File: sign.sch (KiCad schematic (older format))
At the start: 142 parts, among them J1 CONN_01X02, J2 CONN_01X02, J3 CONN_01X02, U1 APA102C_x6, U10 APA102C_x2, U100 APA102C_x6, U101 APA102C_x4, U102 APA102C_x2, U103 APA102C_x1, U104 APA102C_x3, U105 APA102C_x5, U106 APA102C_x2, U107 APA102C_x3, U108 APA102C_x10, U109 APA102C_x9, U11 APA102C_x2, U110 APA102C_x3, U111 APA102C_x12, U112 APA102C_x16, U113 APA102C_x8, U114 APA102C_x13, U115 APA102C_x3, U116 APA102C_x6, U117 APA102C_x3, U118 APA102C_x6, U119 APA102C_x3, U12 APA102C_x2, U120 APA102C_x2, U121 APA102C_x6, U122 APA102C_x3, U123 APA102C_x6, U124 APA102C_x7, U125 APA102C_x12, U126 APA102C_x6, U127 APA102C_x11, U128 APA102C_x4, U129 APA102C_x6, U13 APA102C_x2, U130 APA102C_x2, U131 APA102C_x2, U132 APA102C_x3, U133 APA102C_x1, U134 APA102C_x3, U135 APA102C_x3, U136 APA102C_x12, U137 APA102C_x12, U138 APA102C_x9, U139 APA102C_x4, U14 APA102C_x3, U15 APA102C_x3, U16 APA102C_x3, U17 APA102C_x3, U18 APA102C_x5, U19 APA102C_x6, U2 APA102C_x8, U20 APA102C_x2, U21 APA102C_x7, U22 APA102C_x5, U23 APA102C_x7, U24 APA102C_x3, U25 APA102C_x2, U26 APA102C_x7, U27 APA102C_x2, U28 APA102C_x3, U29 APA102C_x5, U3 APA102C_x11, U30 APA102C_x2, U31 APA102C_x5, U32 APA102C_x2, U33 APA102C_x8, U34 APA102C_x9, U35 APA102C_x3, U36 APA102C_x2, U37 APA102C_x5, U38 APA102C_x11, U39 APA102C_x6, U4 APA102C_x6, U40 APA102C_x4, U41 APA102C_x5, U42 APA102C_x3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

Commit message: Start auto-generating PCB layout.
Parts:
- removed J1, J2, J3: CONN_01X02, symbol CONN_01X02
- removed U1: APA102C_x6, symbol APA102C_x6
- added U139: APA102C_x4, symbol APA102C_x4
- U1: renamed from U2; value APA102C_x8 -> APA102C_x6; symbol APA102C_x8 -> APA102C_x6
- U100: renamed from U101; value APA102C_x4 -> APA102C_x6; symbol APA102C_x4 -> APA102C_x6
- U101: renamed from U102; value APA102C_x2 -> APA102C_x4; symbol APA102C_x2 -> APA102C_x4
- U102: renamed from U103; value APA102C_x1 -> APA102C_x2; symbol APA102C_x1 -> APA102C_x2
- U103: renamed from U104; value APA102C_x3 -> APA102C_x1; symbol APA102C_x3 -> APA102C_x1
- U104: renamed from U105; value APA102C_x5 -> APA102C_x3; symbol APA102C_x5 -> APA102C_x3
- U105: renamed from U106; value APA102C_x2 -> APA102C_x5; symbol APA102C_x2 -> APA102C_x5
- U106: renamed from U107; value APA102C_x3 -> APA102C_x2; symbol APA102C_x3 -> APA102C_x2
- U107: renamed from U108; value APA102C_x10 -> APA102C_x3; symbol APA102C_x10 -> APA102C_x3
- U108: renamed from U109; value APA102C_x9 -> APA102C_x10; symbol APA102C_x9 -> APA102C_x10
- U109: renamed from U110; value APA102C_x3 -> APA102C_x9; symbol APA102C_x3 -> APA102C_x9
- U110: renamed from U111; value APA102C_x12 -> APA102C_x3; symbol APA102C_x12 -> APA102C_x3
- U111: renamed from U112; value APA102C_x16 -> APA102C_x12; symbol APA102C_x16 -> APA102C_x12
- U112: renamed from U113; value APA102C_x8 -> APA102C_x16; symbol APA102C_x8 -> APA102C_x16
- U113: renamed from U114; value APA102C_x13 -> APA102C_x8; symbol APA102C_x13 -> APA102C_x8
- U114: renamed from U115; value APA102C_x3 -> APA102C_x13; symbol APA102C_x3 -> APA102C_x13
- U115: renamed from U116; value APA102C_x6 -> APA102C_x3; symbol APA102C_x6 -> APA102C_x3
- U116: renamed from U117; value APA102C_x3 -> APA102C_x6; symbol APA102C_x3 -> APA102C_x6
- U117: renamed from U118; value APA102C_x6 -> APA102C_x3; symbol APA102C_x6 -> APA102C_x3
- U118: renamed from U119; value APA102C_x3 -> APA102C_x6; symbol APA102C_x3 -> APA102C_x6
- U119: renamed from U120; value APA102C_x2 -> APA102C_x3; symbol APA102C_x2 -> APA102C_x3
- U120: renamed from U121; value APA102C_x6 -> APA102C_x2; symbol APA102C_x6 -> APA102C_x2
- U121: renamed from U122; value APA102C_x3 -> APA102C_x6; symbol APA102C_x3 -> APA102C_x6
- U122: renamed from U123; value APA102C_x6 -> APA102C_x3; symbol APA102C_x6 -> APA102C_x3
- U123: renamed from U124; value APA102C_x7 -> APA102C_x6; symbol APA102C_x7 -> APA102C_x6
- U124: renamed from U125; value APA102C_x12 -> APA102C_x7; symbol APA102C_x12 -> APA102C_x7
- U125: renamed from U126; value APA102C_x6 -> APA102C_x12; symbol APA102C_x6 -> APA102C_x12
- U126: renamed from U127; value APA102C_x11 -> APA102C_x6; symbol APA102C_x11 -> APA102C_x6
- U127: renamed from U128; value APA102C_x4 -> APA102C_x11; symbol APA102C_x4 -> APA102C_x11
- U128: renamed from U129; value APA102C_x6 -> APA102C_x4; symbol APA102C_x6 -> APA102C_x4
- U129: renamed from U130; value APA102C_x2 -> APA102C_x6; symbol APA102C_x2 -> APA102C_x6
- U13: renamed from U14; value APA102C_x3 -> APA102C_x2; symbol APA102C_x3 -> APA102C_x2
- U131: renamed from U132; value APA102C_x3 -> APA102C_x2; symbol APA102C_x3 -> APA102C_x2
- U132: renamed from U133; value APA102C_x1 -> APA102C_x3; symbol APA102C_x1 -> APA102C_x3
- U133: renamed from U134; value APA102C_x3 -> APA102C_x1; symbol APA102C_x3 -> APA102C_x1
- U135: renamed from U136; value APA102C_x12 -> APA102C_x3; symbol APA102C_x12 -> APA102C_x3
- U137: renamed from U138; value APA102C_x9 -> APA102C_x12; symbol APA102C_x9 -> APA102C_x12
- U138: renamed from U139; value APA102C_x4 -> APA102C_x9; symbol APA102C_x4 -> APA102C_x9
- U17: renamed from U18; value APA102C_x5 -> APA102C_x3; symbol APA102C_x5 -> APA102C_x3
- U18: renamed from U19; value APA102C_x6 -> APA102C_x5; symbol APA102C_x6 -> APA102C_x5
- U19: renamed from U20; value APA102C_x2 -> APA102C_x6; symbol APA102C_x2 -> APA102C_x6
- U2: renamed from U3; value APA102C_x11 -> APA102C_x8; symbol APA102C_x11 -> APA102C_x8
- U20: renamed from U21; value APA102C_x7 -> APA102C_x2; symbol APA102C_x7 -> APA102C_x2
- U21: renamed from U22; value APA102C_x5 -> APA102C_x7; symbol APA102C_x5 -> APA102C_x7
- U22: renamed from U23; value APA102C_x7 -> APA102C_x5; symbol APA102C_x7 -> APA102C_x5
- U23: renamed from U24; value APA102C_x3 -> APA102C_x7; symbol APA102C_x3 -> APA102C_x7
- U24: renamed from U25; value APA102C_x2 -> APA102C_x3; symbol APA102C_x2 -> APA102C_x3
- U25: renamed from U26; value APA102C_x7 -> APA102C_x2; symbol APA102C_x7 -> APA102C_x2
- U26: renamed from U27; value APA102C_x2 -> APA102C_x7; symbol APA102C_x2 -> APA102C_x7
- U27: renamed from U28; value APA102C_x3 -> APA102C_x2; symbol APA102C_x3 -> APA102C_x2
- U28: renamed from U29; value APA102C_x5 -> APA102C_x3; symbol APA102C_x5 -> APA102C_x3
- U29: renamed from U30; value APA102C_x2 -> APA102C_x5; symbol APA102C_x2 -> APA102C_x5
- U3: renamed from U4; value APA102C_x6 -> APA102C_x11; symbol APA102C_x6 -> APA102C_x11
- U30: renamed from U31; value APA102C_x5 -> APA102C_x2; symbol APA102C_x5 -> APA102C_x2
- U31: renamed from U32; value APA102C_x2 -> APA102C_x5; symbol APA102C_x2 -> APA102C_x5
- U32: renamed from U33; value APA102C_x8 -> APA102C_x2; symbol APA102C_x8 -> APA102C_x2
- U33: renamed from U34; value APA102C_x9 -> APA102C_x8; symbol APA102C_x9 -> APA102C_x8
- U34: renamed from U35; value APA102C_x3 -> APA102C_x9; symbol APA102C_x3 -> APA102C_x9
- U35: renamed from U36; value APA102C_x2 -> APA102C_x3; symbol APA102C_x2 -> APA102C_x3
- U36: renamed from U37; value APA102C_x5 -> APA102C_x2; symbol APA102C_x5 -> APA102C_x2
- U37: renamed from U38; value APA102C_x11 -> APA102C_x5; symbol APA102C_x11 -> APA102C_x5
- U38: renamed from U39; value APA102C_x6 -> APA102C_x11; symbol APA102C_x6 -> APA102C_x11
- U39: renamed from U40; value APA102C_x4 -> APA102C_x6; symbol APA102C_x4 -> APA102C_x6
- U4: renamed from U5; value APA102C_x3 -> APA102C_x6; symbol APA102C_x3 -> APA102C_x6
- U40: renamed from U41; value APA102C_x5 -> APA102C_x4; symbol APA102C_x5 -> APA102C_x4
- U41: renamed from U42; value APA102C_x3 -> APA102C_x5; symbol APA102C_x3 -> APA102C_x5
- U42: renamed from U43; value APA102C_x4 -> APA102C_x3; symbol APA102C_x4 -> APA102C_x3
- U43: renamed from U44; value APA102C_x6 -> APA102C_x4; symbol APA102C_x6 -> APA102C_x4
- U44: renamed from U45; value APA102C_x4 -> APA102C_x6; symbol APA102C_x4 -> APA102C_x6
- U45: renamed from U46; value APA102C_x3 -> APA102C_x4; symbol APA102C_x3 -> APA102C_x4
- U46: renamed from U47; value APA102C_x4 -> APA102C_x3; symbol APA102C_x4 -> APA102C_x3
- U47: renamed from U48; value APA102C_x2 -> APA102C_x4; symbol APA102C_x2 -> APA102C_x4
- U48: renamed from U49; value APA102C_x3 -> APA102C_x2; symbol APA102C_x3 -> APA102C_x2
- U49: renamed from U50; value APA102C_x2 -> APA102C_x3; symbol APA102C_x2 -> APA102C_x3
- U51: renamed from U52; value APA102C_x3 -> APA102C_x2; symbol APA102C_x3 -> APA102C_x2
- U55: renamed from U56; value APA102C_x7 -> APA102C_x3; symbol APA102C_x7 -> APA102C_x3
- U56: renamed from U57; value APA102C_x4 -> APA102C_x7; symbol APA102C_x4 -> APA102C_x7
- U57: renamed from U58; value APA102C_x12 -> APA102C_x4; symbol APA102C_x12 -> APA102C_x4
- U58: renamed from U59; value APA102C_x3 -> APA102C_x12; symbol APA102C_x3 -> APA102C_x12
- U59: renamed from U60; value APA102C_x14 -> APA102C_x3; symbol APA102C_x14 -> APA102C_x3
- U6: renamed from U7; value APA102C_x2 -> APA102C_x3; symbol APA102C_x2 -> APA102C_x3
- U60: renamed from U61; value APA102C_x3 -> APA102C_x14; symbol APA102C_x3 -> APA102C_x14
- U61: renamed from U62; value APA102C_x10 -> APA102C_x3; symbol APA102C_x10 -> APA102C_x3
- U62: renamed from U63; value APA102C_x4 -> APA102C_x10; symbol APA102C_x4 -> APA102C_x10
- U63: renamed from U64; value APA102C_x6 -> APA102C_x4; symbol APA102C_x6 -> APA102C_x4
- U64: renamed from U65; value APA102C_x9 -> APA102C_x6; symbol APA102C_x9 -> APA102C_x6
- U65: renamed from U66; value APA102C_x1 -> APA102C_x9; symbol APA102C_x1 -> APA102C_x9
- U66: renamed from U67; value APA102C_x13 -> APA102C_x1; symbol APA102C_x13 -> APA102C_x1
- U67: renamed from U68; value APA102C_x5 -> APA102C_x13; symbol APA102C_x5 -> APA102C_x13
- U68: renamed from U69; value APA102C_x13 -> APA102C_x5; symbol APA102C_x13 -> APA102C_x5
- U69: renamed from U70; value APA102C_x9 -> APA102C_x13; symbol APA102C_x9 -> APA102C_x13
- U7: renamed from U8; value APA102C_x3 -> APA102C_x2; symbol APA102C_x3 -> APA102C_x2
- U70: renamed from U71; value APA102C_x2 -> APA102C_x9; symbol APA102C_x2 -> APA102C_x9
- U71: renamed from U72; value APA102C_x8 -> APA102C_x2; symbol APA102C_x8 -> APA102C_x2
- U72: renamed from U73; value APA102C_x11 -> APA102C_x8; symbol APA102C_x11 -> APA102C_x8
- U73: renamed from U74; value APA102C_x3 -> APA102C_x11; symbol APA102C_x3 -> APA102C_x11
- U75: renamed from U76; value APA102C_x5 -> APA102C_x3; symbol APA102C_x5 -> APA102C_x3
- U76: renamed from U77; value APA102C_x3 -> APA102C_x5; symbol APA102C_x3 -> APA102C_x5
- U77: renamed from U78; value APA102C_x2 -> APA102C_x3; symbol APA102C_x2 -> APA102C_x3
- U78: renamed from U79; value APA102C_x4 -> APA102C_x2; symbol APA102C_x4 -> APA102C_x2
- U79: renamed from U80; value APA102C_x3 -> APA102C_x4; symbol APA102C_x3 -> APA102C_x4
- U80: renamed from U81; value APA102C_x2 -> APA102C_x3; symbol APA102C_x2 -> APA102C_x3
- U81: renamed from U82; value APA102C_x3 -> APA102C_x2; symbol APA102C_x3 -> APA102C_x2
- U82: renamed from U83; value APA102C_x2 -> APA102C_x3; symbol APA102C_x2 -> APA102C_x3
- U83: renamed from U84; value APA102C_x5 -> APA102C_x2; symbol APA102C_x5 -> APA102C_x2
- U84: renamed from U85; value APA102C_x3 -> APA102C_x5; symbol APA102C_x3 -> APA102C_x5
- U86: renamed from U87; value APA102C_x10 -> APA102C_x3; symbol APA102C_x10 -> APA102C_x3
- U87: renamed from U88; value APA102C_x3 -> APA102C_x10; symbol APA102C_x3 -> APA102C_x10
- U88: renamed from U89; value APA102C_x7 -> APA102C_x3; symbol APA102C_x7 -> APA102C_x3
- U89: renamed from U90; value APA102C_x12 -> APA102C_x7; symbol APA102C_x12 -> APA102C_x7
- U9: renamed from U10; value APA102C_x2 -> APA102C_x3; symbol APA102C_x2 -> APA102C_x3
- U91: renamed from U92; value APA102C_x2 -> APA102C_x12; symbol APA102C_x2 -> APA102C_x12
- U92: renamed from U93; value APA102C_x8 -> APA102C_x2; symbol APA102C_x8 -> APA102C_x2
- U93: renamed from U94; value APA102C_x14 -> APA102C_x8; symbol APA102C_x14 -> APA102C_x8
- U94: renamed from U95; value APA102C_x3 -> APA102C_x14; symbol APA102C_x3 -> APA102C_x14
- U96: renamed from U97; value APA102C_x10 -> APA102C_x3; symbol APA102C_x10 -> APA102C_x3
- U97: renamed from U98; value APA102C_x3 -> APA102C_x10; symbol APA102C_x3 -> APA102C_x10
- U98: renamed from U99; value APA102C_x2 -> APA102C_x3; symbol APA102C_x2 -> APA102C_x3
- U99: renamed from U100; value APA102C_x6 -> APA102C_x2; symbol APA102C_x6 -> APA102C_x2
- renumbered U11 to U10, U12 to U11, U13 to U12, U131 to U130, U135 to U134, U137 to U136, U15 to U14, U16 to U15, U17 to U16, U6 to U5, U51 to U50, U53 to U52, U54 to U53, U55 to U54, U75 to U74, U9 to U8, U86 to U85, U91 to U90, U96 to U95
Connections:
- no-connect marks 2 -> 0
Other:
- moved on the sheet: U1, U10, U100, U101, U102, U103, U104, U105, U106, U107, U108, U109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

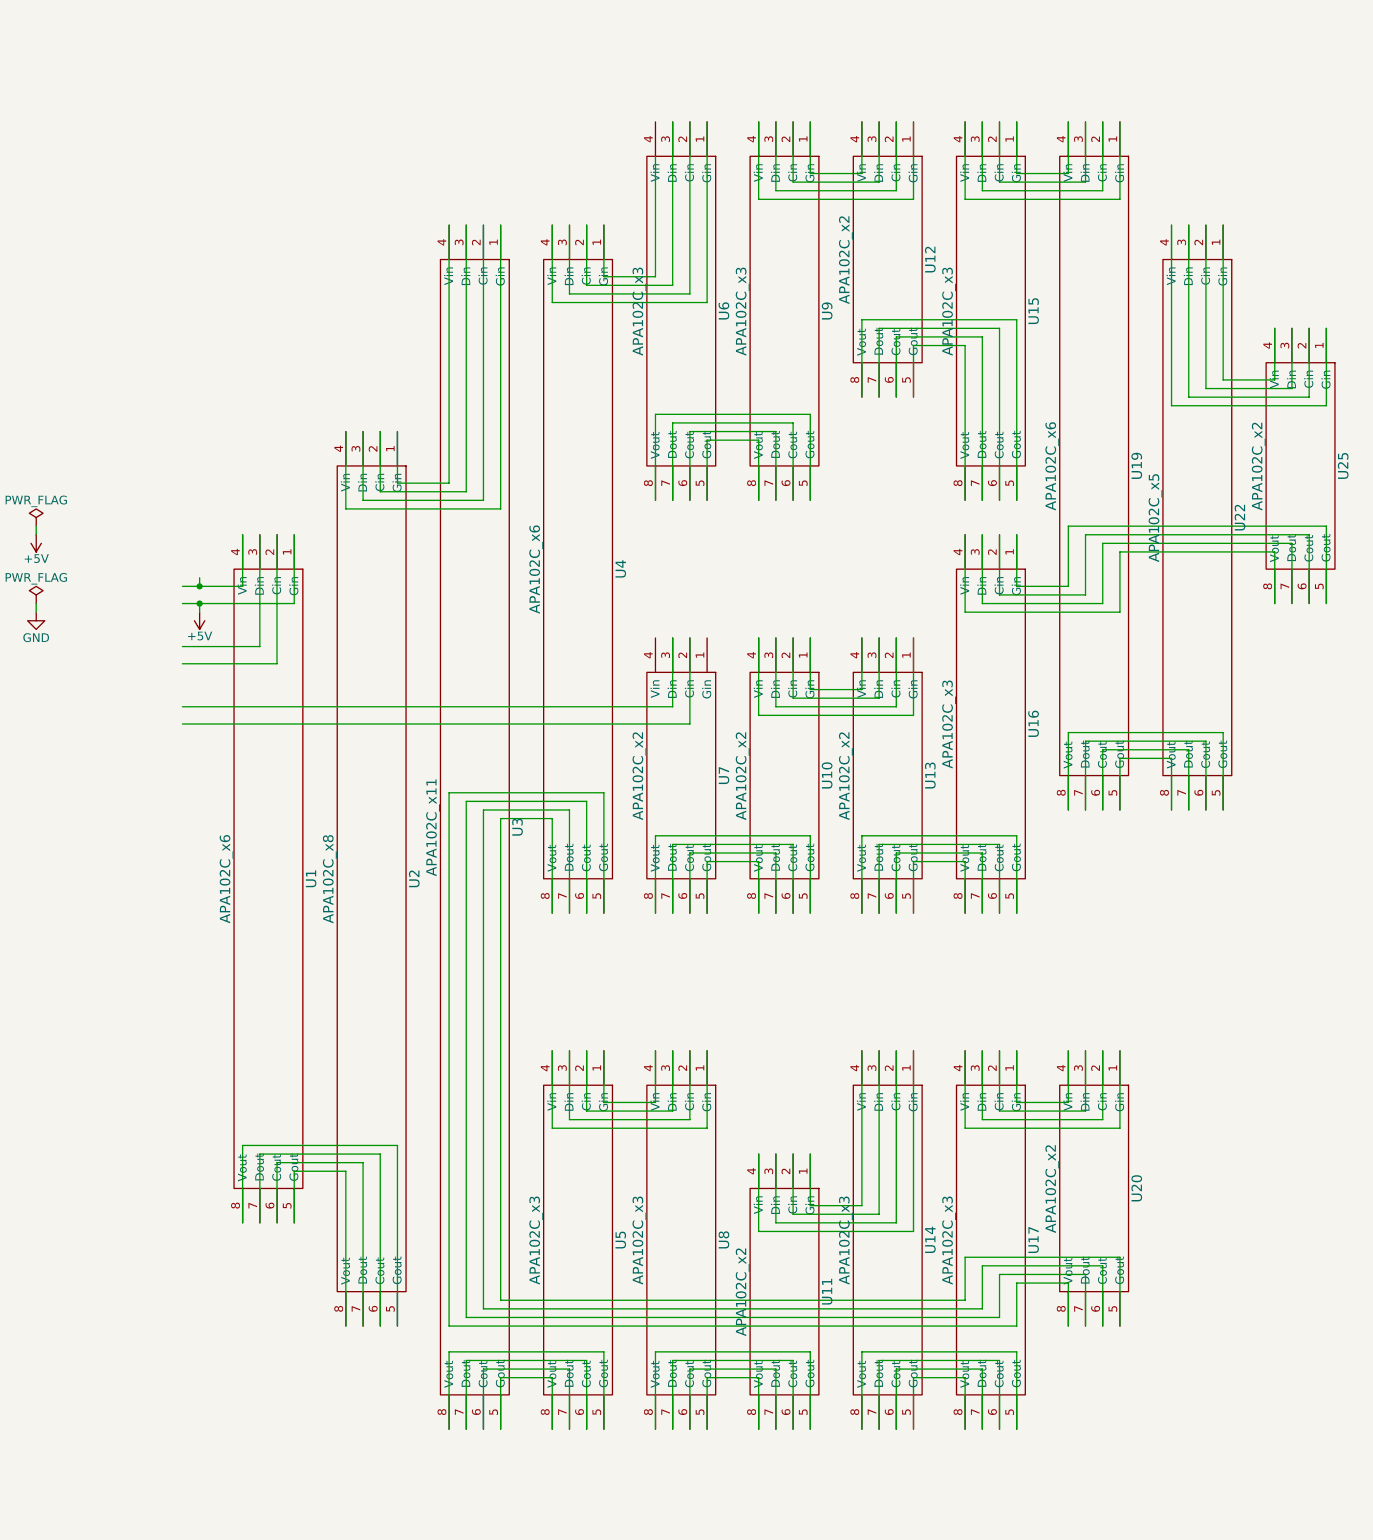
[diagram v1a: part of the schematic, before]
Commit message: Fix layout of 'e'
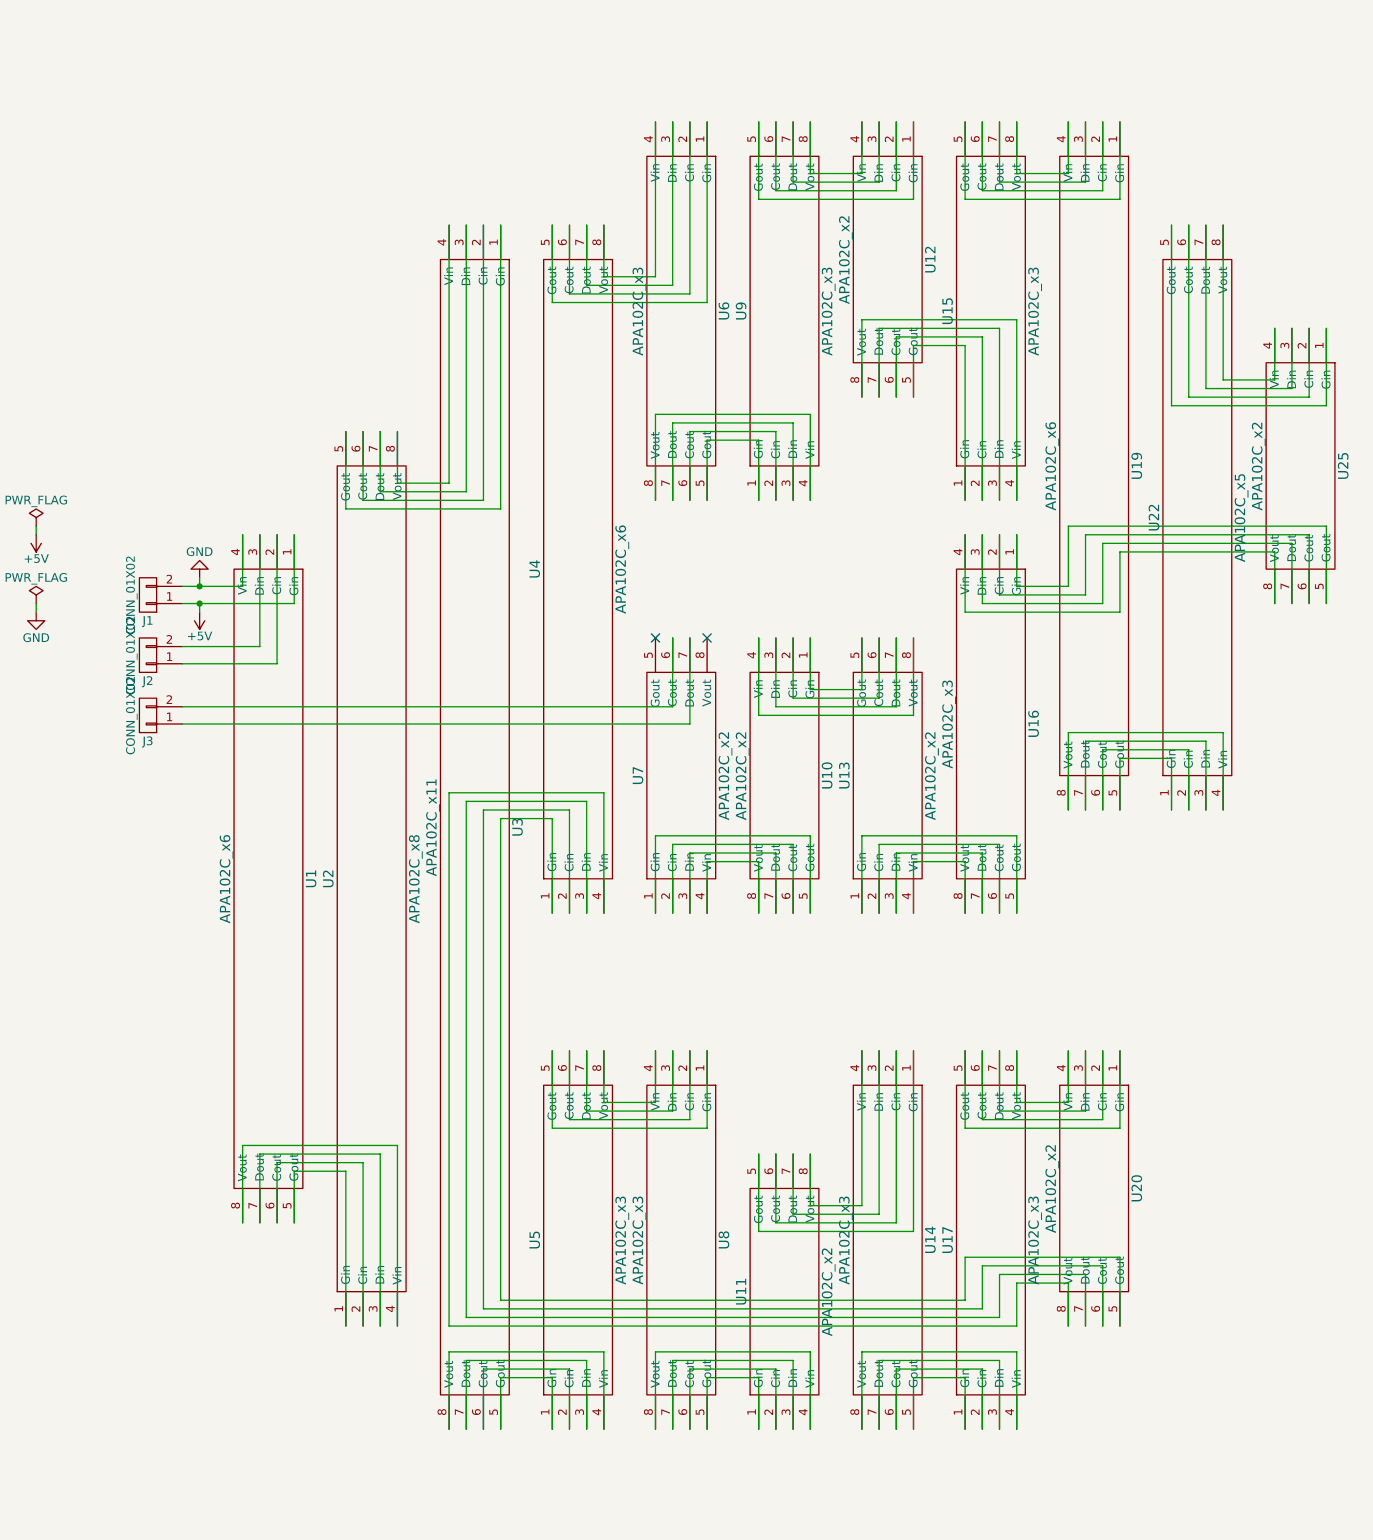
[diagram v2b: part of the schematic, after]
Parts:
- added J1, J2, J3: CONN_01X02, Pin_Headers:Pin_Header_Straight_1x02, symbol CONN_01X02
- U1, U100, U116, U118, U121, U123, U126, U129, U19, U39, U4, U44, U64: footprint (none) -> apa102c_72m:APA102C_72m_x6
- U10, U102, U106, U11, U12, U120, U13, U130, U131, U20, U25, U27, U30, U32, U36, U48, U50, U51, U7, U71, U78, U81, U83, U92, U99: footprint (none) -> apa102c_72m:APA102C_72m_x2
- U101, U128, U139, U40, U43, U45, U47, U57, U63, U79: footprint (none) -> apa102c_72m:APA102C_72m_x4
- U103, U133, U66: footprint (none) -> apa102c_72m:APA102C_72m_x1
- U104, U107, U110, U115, U117, U119, U122, U132, U134, U135, U14, U15, U16, U17, U24, U28, U35, U42, U46, U49, U5, U52, U53, U54, U55, U59, U6, U61, U74, U75, U77, U8, U80, U82, U85, U86, U88, U9, U95, U96, U98: footprint (none) -> apa102c_72m:APA102C_72m_x3
- U105, U18, U22, U29, U31, U37, U41, U68, U76, U84: footprint (none) -> apa102c_72m:APA102C_72m_x5
- U108, U62, U87, U97: footprint (none) -> apa102c_72m:APA102C_72m_x10
- U109, U138, U34, U65, U70: footprint (none) -> apa102c_72m:APA102C_72m_x9
- U111, U125, U136, U137, U58, U90, U91: footprint (none) -> apa102c_72m:APA102C_72m_x12
- U112: footprint (none) -> apa102c_72m:APA102C_72m_x16
- U113, U2, U33, U72, U93: footprint (none) -> apa102c_72m:APA102C_72m_x8
- U114, U67, U69: footprint (none) -> apa102c_72m:APA102C_72m_x13
- U124, U21, U23, U26, U56, U89: footprint (none) -> apa102c_72m:APA102C_72m_x7
- U127, U3, U38, U73: footprint (none) -> apa102c_72m:APA102C_72m_x11
- U60, U94: footprint (none) -> apa102c_72m:APA102C_72m_x14
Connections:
- no-connect marks 0 -> 2
